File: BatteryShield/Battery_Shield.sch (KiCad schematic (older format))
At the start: 0 parts

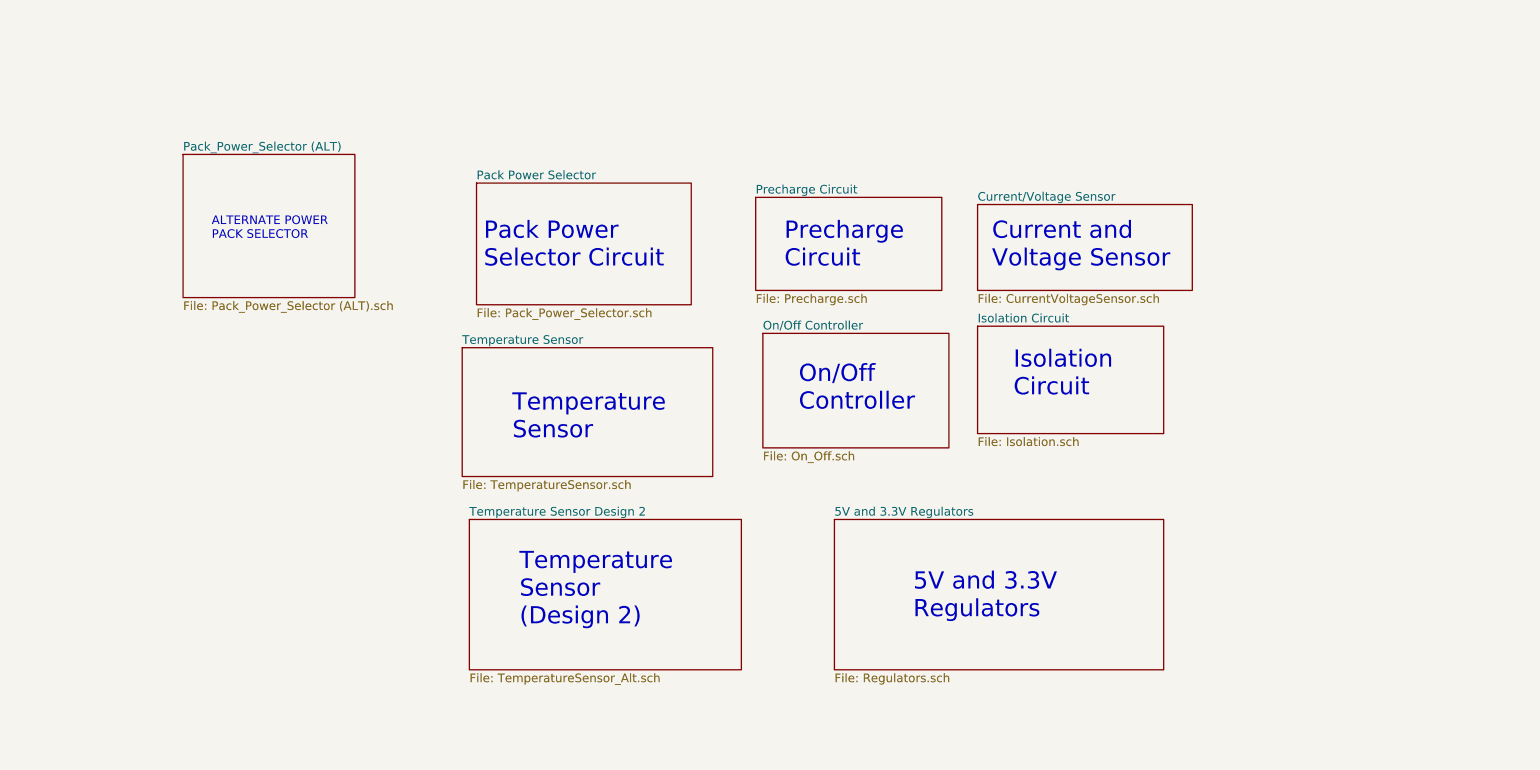
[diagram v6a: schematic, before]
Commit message: Added two pages, cleaned up net names
Cleaned up net names. Added protection/grounding and BBB interface socket. Additional work needs to be done with grounding/mounting holes and 37V rail reverse current protection.
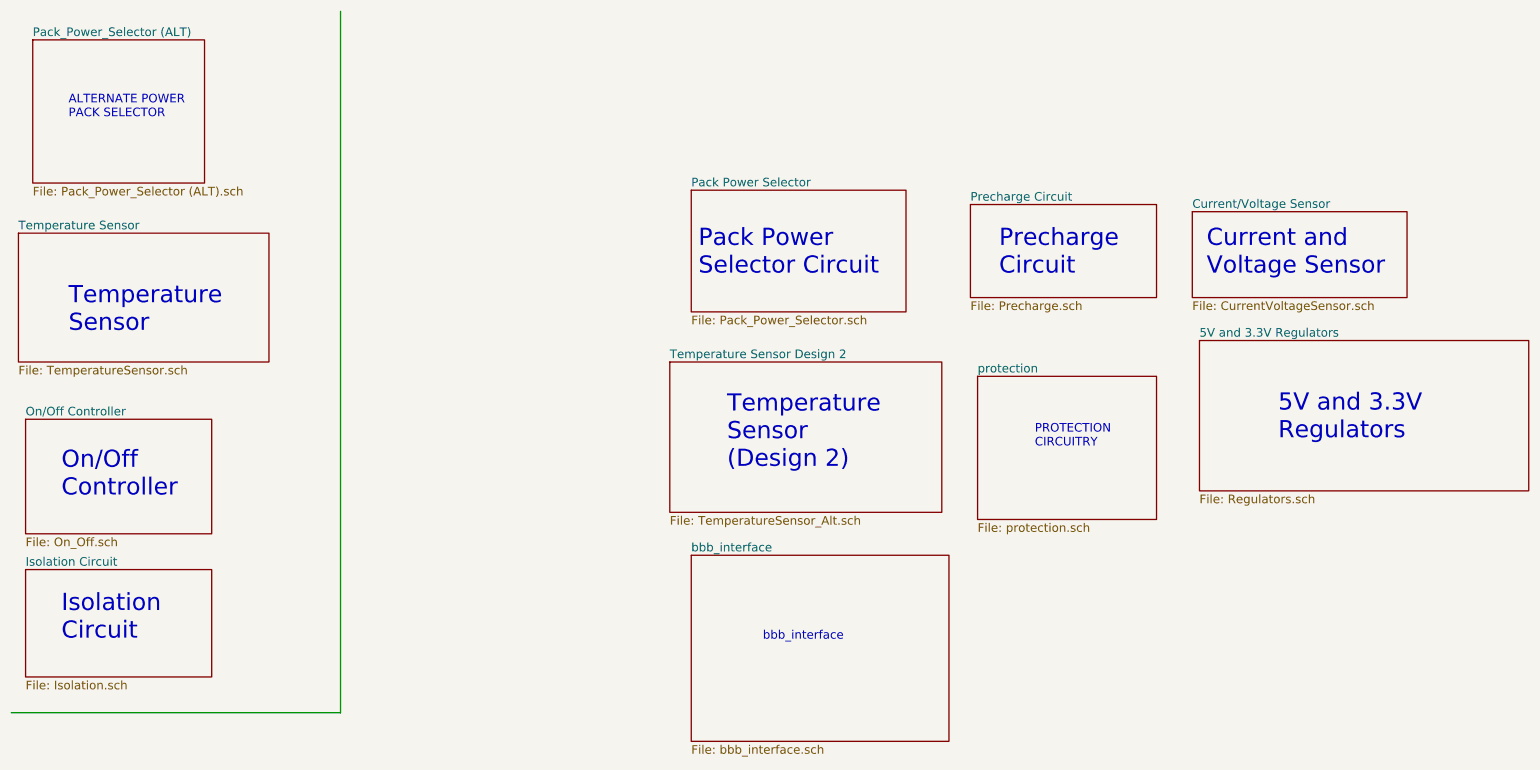
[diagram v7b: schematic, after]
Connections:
- wire segments 0 -> 2
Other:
- note added: "PROTECTION\nCIRCUITRY\n"
- note added: "bbb_interface\n"
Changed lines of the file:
@@
 $Descr A4 11693 8268
 encoding utf-8
-Sheet 1 10
+Sheet 1 12
 Title ""
 Date ""
@@
 $EndDescr
 $Sheet
-S 7300 1850 1500 600
+S 8800 1900 1500 600
 U 5A64EF94
 F0 "Current/Voltage Sensor" 60
@@
 $EndSheet
 $Sheet
-S 7300 2700 1300 750
+S 650  4400 1300 750
 U 5A668B9B
 F0 "Isolation Circuit" 60
@@
 $EndSheet
 $Sheet
-S 5750 1800 1300 650
+S 7250 1850 1300 650
 U 5A668BC0
 F0 "Precharge Circuit" 60
@@
 $EndSheet
 $Sheet
-S 5800 2750 1300 800
+S 650  3350 1300 800
 U 5A668BD8
 F0 "On/Off Controller" 60
@@
 $EndSheet
 $Sheet
-S 3800 1700 1500 850
+S 5300 1750 1500 850
 U 5A668BFB
 F0 "Pack Power Selector" 60
 F1 "Pack_Power_Selector.sch" 60
 $EndSheet
-Text Notes 7400 2300 0    120  ~ 0
+Text Notes 8900 2350 0    120  ~ 0
 Current and \nVoltage Sensor
-Text Notes 7550 3200 0    120  ~ 0
+Text Notes 900  4900 0    120  ~ 0
 Isolation\nCircuit
-Text Notes 6050 3300 0    120  ~ 0
+Text Notes 900  3900 0    120  ~ 0
 On/Off\nController
-Text Notes 5950 2300 0    120  ~ 0
+Text Notes 7450 2350 0    120  ~ 0
 Precharge\nCircuit
-Text Notes 3850 2300 0    120  ~ 0
+Text Notes 5350 2350 0    120  ~ 0
 Pack Power\nSelector Circuit
 $Sheet
-S 3700 2850 1750 900
+S 600  2050 1750 900
 U 5A767D76
 F0 "Temperature Sensor" 60
 F1 "TemperatureSensor.sch" 60
 $EndSheet
-Text Notes 4050 3500 0    120  ~ 0
+Text Notes 950  2750 0    120  ~ 0
 Temperature\nSensor
 $Sheet
-S 3750 4050 1900 1050
+S 5150 2950 1900 1050
 U 5A8239AC
 F0 "Temperature Sensor Design 2" 60
 F1 "TemperatureSensor_Alt.sch" 60
 $EndSheet
-Text Notes 4100 4800 0    120  ~ 0
+Text Notes 5550 3700 0    120  ~ 0
 Temperature\nSensor\n(Design 2)
 $Sheet
-S 6300 4050 2300 1050
+S 8850 2800 2300 1050
 U 5A86217E
 F0 "5V and 3.3V Regulators" 60
 F1 "Regulators.sch" 60
 $EndSheet
-Text Notes 6850 4750 0    120  ~ 0
+Text Notes 9400 3500 0    120  ~ 0
 5V and 3.3V\nRegulators
 $Sheet
-S 1750 1500 1200 1000
+S 700  700  1200 1000
 U 5B0DE919
 F0 "Pack_Power_Selector (ALT)" 60
 F1 "Pack_Power_Selector (ALT).sch" 60
 $EndSheet
-Text Notes 1950 2100 0    60   ~ 0
+Text Notes 950  1250 0    60   ~ 0
 ALTERNATE POWER\nPACK SELECTOR\n
+$Sheet
+S 7300 3050 1250 1000
+U 5B11F329
+F0 "protection" 60
+F1 "protection.sch" 60
+$EndSheet
+Wire Wire Line
+	2850 500  2850 5400
+Wire Wire Line
+	2850 5400 550  5400
+Text Notes 7700 3550 0    60   ~ 0
+PROTECTION\nCIRCUITRY\n
+$Sheet
+S 5300 4300 1800 1300
+U 5B12079D
+F0 "bbb_interface" 60
+F1 "bbb_interface.sch" 60
+$EndSheet
+Text Notes 5800 4900 0    60   ~ 0
+bbb_interface\n
 $EndSCHEMATC

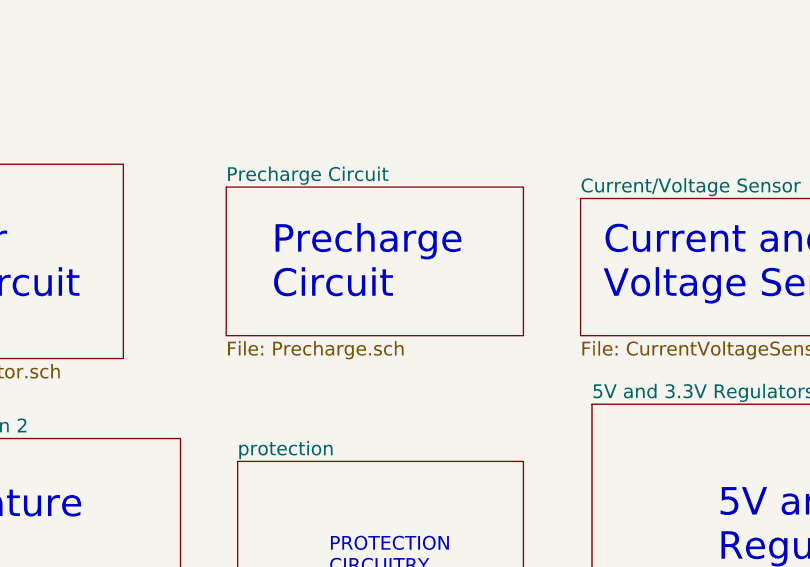
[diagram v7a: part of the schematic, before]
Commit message: Associated a lot of footprints
Now I need to add a lot more :(
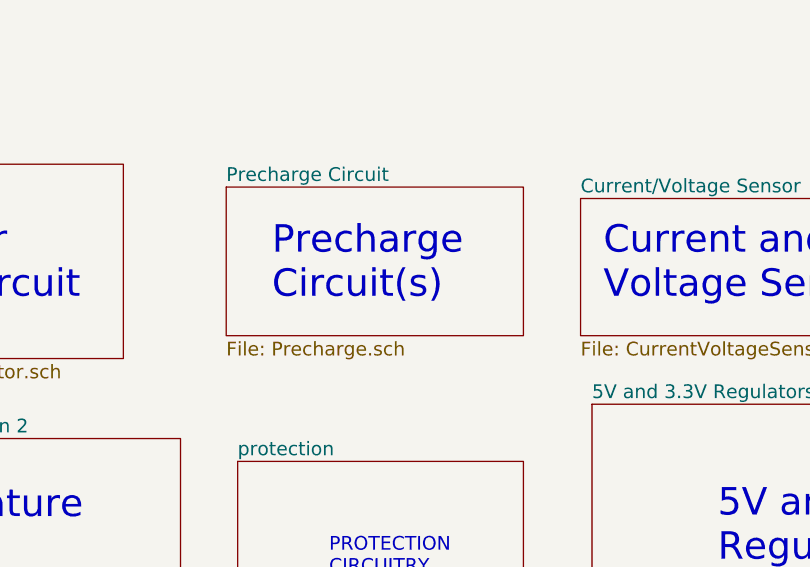
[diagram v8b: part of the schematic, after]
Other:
- note added: "Precharge\nCircuit(s)"
- note removed: "Precharge\nCircuit"
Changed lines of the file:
@@
 On/Off\nController
 Text Notes 7450 2350 0    120  ~ 0
-Precharge\nCircuit
+Precharge\nCircuit(s)
 Text Notes 5350 2350 0    120  ~ 0
 Pack Power\nSelector Circuit
@@
 Text Notes 5550 3700 0    120  ~ 0
 Temperature\nSensor\n(Design 2)
-$Sheet
-S 8850 2800 2300 1050
-U 5A86217E
-F0 "5V and 3.3V Regulators" 60
-F1 "Regulators.sch" 60
-$EndSheet
 Text Notes 9400 3500 0    120  ~ 0
 5V and 3.3V\nRegulators
@@
 Text Notes 5800 4900 0    60   ~ 0
 bbb_interface\n
+$Sheet
+S 8850 2800 2300 1050
+U 5A86217E
+F0 "5V and 3.3V Regulators" 60
+F1 "Regulators.sch" 60
+$EndSheet
 $EndSCHEMATC
